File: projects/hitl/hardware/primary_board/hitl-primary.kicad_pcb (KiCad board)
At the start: 4 copper layers, 108 x 79.7 mm, 131 parts, among them J1 USB-Micro-1981568-1, J10 CONN_01X03, J11 CONN_01X03, J12 CONN_01X03, J13 CONN_01x02, J14 SSW-122-01-G-D, J15 CONN_01x02, J16 CONN_01X03, J17 CONN_01X03, J18 CONN_01X03, J19 CONN_01X03, J2 Barrel_jack, J20 CONN_01X03, J3 MM_F_VT_08_SM, J4 MM_F_VT_08_SM, J5 CONN_01x02, J6 DSub-9, J7 CONN_01X03, J8 CONN_01X03, J9 CONN_01X03, Q1 SSM3K333R, Q2 SSM3K333R, Q3 SSM3K333R, Q4 SSM3K333R, U1 R_500, U2 FT4222H, U3 PCA9306, U4 AD5675, U5 MAX7300AAXT, U6 RU_20_ADI, U7 MCP6001, U8 SOT109-1_NXP, U9 LT3045, Y1 Crystal_12MHz

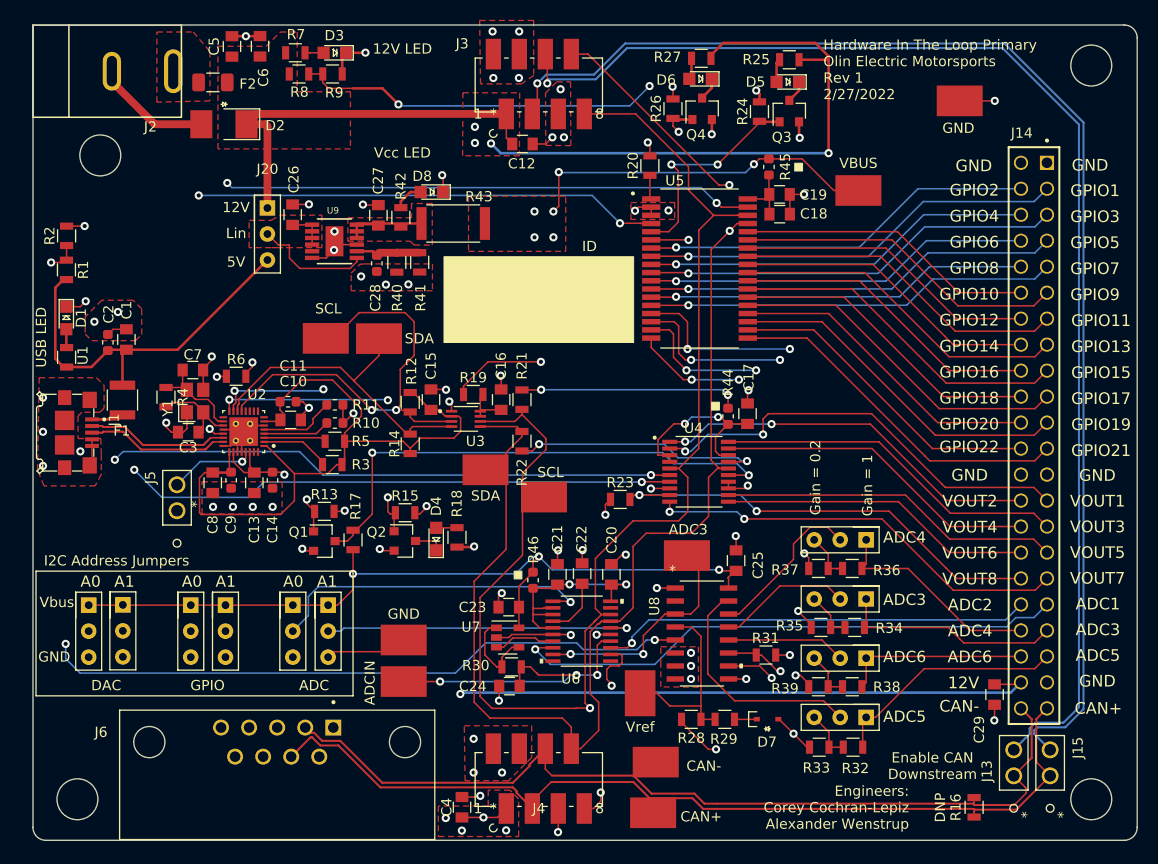
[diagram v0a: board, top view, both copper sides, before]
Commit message: Split schematic into sheets
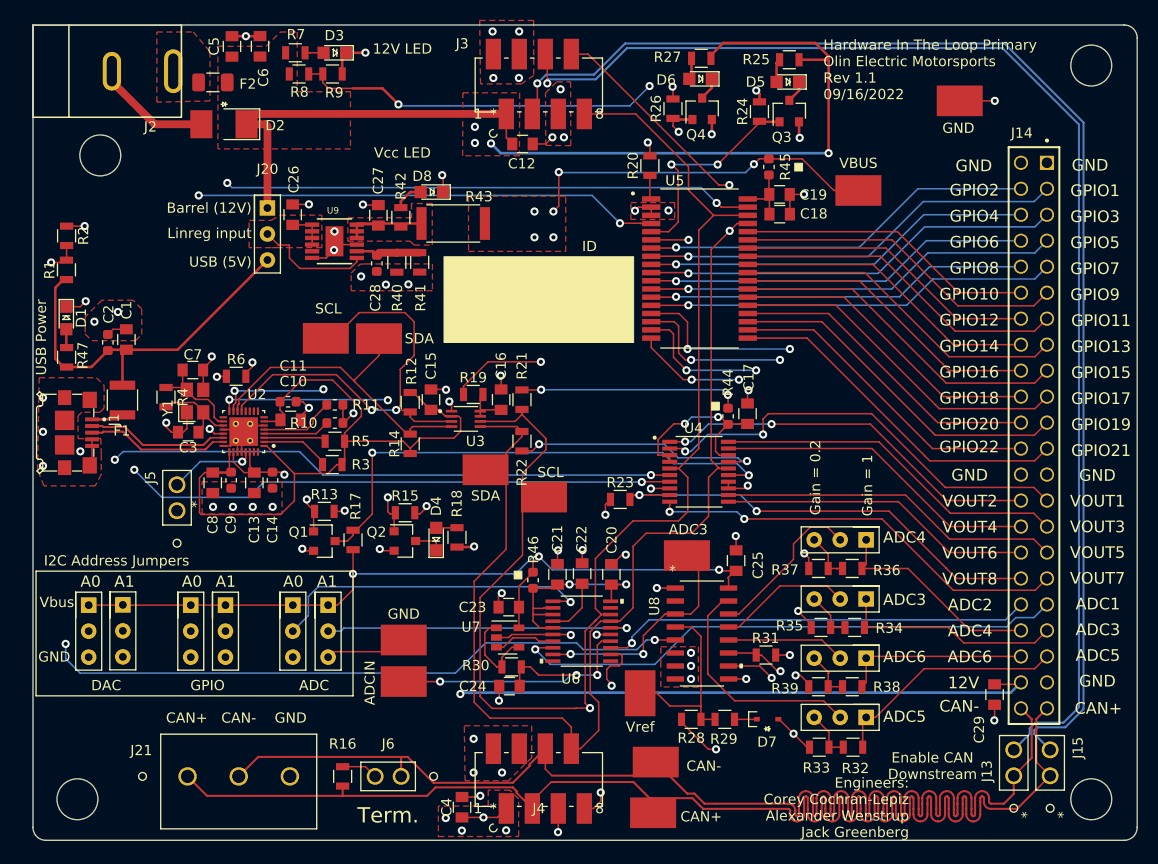
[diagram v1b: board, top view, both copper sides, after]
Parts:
- added J21: Screw_Terminal_01x03, footprints:ScrewPin_1x3, F.Cu at (87.7, 108.0)
- J6: value DSub-9 -> CONN_01x02; footprint footprints:TE_5745781-4 -> footprints:pinheader_1x2
- R16: value R_120_DNP -> R_120
- U6: value RU_20_ADI -> AD7091R-5BRUZ
- U8: value SOT109-1_NXP -> 74HCT4051D
- moved R16 61.8 mm to (102.9, 108.0)
- moved J6 12.6 mm to (108.6, 108.0), turned to 180 degrees
- turned R1 to 90 degrees
- turned R10 to 0 degrees
- turned R2 to -90 degrees
- renumbered U1 to R47
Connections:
- net /ADC-CA0 renamed /ADC Circuitry/ADC-CA0
- net /ADC-CA1 renamed /ADC Circuitry/ADC-CA1
- net /ADC1 renamed /ADC Circuitry/ADC1
- net /ADC2 renamed /ADC Circuitry/ADC2
- net /ADC4 renamed /ADC Circuitry/ADC_SELF_TEST
- net /Analog-MUX2 renamed /ADC Circuitry/ADC4
- net /Analog-MUX3 renamed /ADC Circuitry/ADC5
- net /Analog-MUX4 renamed /ADC Circuitry/ADC6
- net /Analog-MUX5 renamed /ADC Circuitry/ADC7
- net /CAN_AWAY+ renamed /Connectors/CAN_AWAY+
- net /CAN_AWAY- renamed /Connectors/CAN_AWAY-
- net /D+ renamed /USB->I2C/D+
- net /D- renamed /USB->I2C/D-
- net /DAC-A0 renamed /DAC/DAC-A0
- net /DAC-A1 renamed /DAC/DAC-A1
- net /DAC-LDAC renamed Net-(Q1-Pad3)
- net /FT-GPIO2 renamed /DAC/DAC-LDAC
- net /FT-GPIO3 renamed Net-(Q2-Pad1)
- net /FT-VPP renamed /USB->I2C/FT-VPP
- net /GPIO-10 renamed /Connectors/GPIO10
- net /GPIO-11 renamed /Connectors/GPIO11
- net /GPIO-12 renamed /Connectors/GPIO12
- net /GPIO-13 renamed /Connectors/GPIO13
- net /GPIO-14 renamed /Connectors/GPIO14
- net /GPIO-15 renamed /Connectors/GPIO15
- net /GPIO-16 renamed /Connectors/GPIO16
- net /GPIO-17 renamed /Connectors/GPIO17
- net /GPIO-18 renamed /Connectors/GPIO18
- net /GPIO-19 renamed /Connectors/GPIO19
- net /GPIO-20 renamed /Connectors/GPIO20
- net /GPIO-21 renamed /Connectors/GPIO21
- net /GPIO-22 renamed /Connectors/GPIO22
- net /GPIO-23 renamed /Connectors/GPIO23
- net /GPIO-24 renamed /Connectors/GPIO24
- net /GPIO-25 renamed /Connectors/GPIO25
- net /GPIO-26 renamed /Connectors/GPIO26
- net /GPIO-27 renamed /Connectors/GPIO27
- net /GPIO-28 renamed /Connectors/GPIO28
- net /GPIO-29 renamed /Connectors/GPIO29
- net /GPIO-30 renamed /Connectors/GPIO30
- net /GPIO-31 renamed /Connectors/GPIO31
- net /GPIO-4 renamed /Connectors/GPIO4
- net /GPIO-5 renamed /Connectors/GPIO5
- net /GPIO-6 renamed /Connectors/GPIO6
- net /GPIO-7 renamed /Connectors/GPIO7
- net /GPIO-8 renamed /Connectors/GPIO8
- net /GPIO-9 renamed /Connectors/GPIO9
- net /GPIO-AD0 renamed /GPIO/GPIO-AD0
- net /GPIO-AD1 renamed /GPIO/GPIO-AD1
- net /SCL renamed /Connectors/SCL
- net /SCL-FT renamed /USB->I2C/SDA
- net /SDA renamed /Connectors/SDA
- net /SDA-FT renamed /USB->I2C/SCL
- net /VOUT-1 renamed /Connectors/DAC1
- net /VOUT-2 renamed /Connectors/DAC2
- net /VOUT-3 renamed /Connectors/DAC3
- net /VOUT-4 renamed /Connectors/DAC4
- net /VOUT-5 renamed /Connectors/DAC5
- net /VOUT-6 renamed /Connectors/DAC6
- net /VOUT-7 renamed /Connectors/DAC7
- net /VOUT-8 renamed /Connectors/DAC8
- J13 pad 1: /CAN- -> /Connectors/CAN_N
- J14 pad 37: /Analog-MUX1 -> /ADC Circuitry/ADC3
- J14 pad 43: /CAN+ -> /Connectors/CAN_P
- J14 pad 44: /CAN- -> /Connectors/CAN_N
- J15 pad 1: /CAN+ -> /Connectors/CAN_P
- J17 pad 1: /Analog-MUX1 -> /ADC Circuitry/ADC3
- J4 pad 4: /CAN+ -> /Connectors/CAN_P
- J4 pad 5: /CAN- -> /Connectors/CAN_N
- J6 pad 1: Net-(J6-Pad1) -> /Connectors/CAN_N
- J6 pad 2: /CAN- -> Net-(J6-Pad2)
- R1 pad 1: /Analog-MUX6 -> +5V
- R1 pad 2: +5V -> /ADC Circuitry/Analog-MUX6
- R10 pad 1: GND -> Net-(R10-Pad1)
- R10 pad 2: Net-(R10-Pad2) -> GND
- R16 pad 1: /CAN+ -> /Connectors/CAN_P
- R16 pad 2: /CAN- -> Net-(J6-Pad2)
- R2 pad 1: /Analog-MUX6 -> GND
- R2 pad 2: GND -> /ADC Circuitry/Analog-MUX6
- R34 pad 1: /Analog-MUX1 -> /ADC Circuitry/ADC3
- TP11 pad 1: /ADC Circuitry/ADC3 -> /ADC Circuitry/ADC_MUX
- TP2 pad 1: /CAN+ -> /Connectors/CAN_P
- TP3 pad 1: /CAN- -> /Connectors/CAN_N
- U2 pad 10: Net-(U2-Pad10) -> unconnected-(U2-Pad10)
- U2 pad 11: Net-(U2-Pad11) -> unconnected-(U2-Pad11)
- U2 pad 12: Net-(U2-Pad12) -> unconnected-(U2-Pad12)
- U2 pad 17: Net-(U2-Pad17) -> unconnected-(U2-Pad17)
- U2 pad 31: Net-(U2-Pad31) -> unconnected-(U2-Pad31)
- U2 pad 32: Net-(U2-Pad32) -> unconnected-(U2-Pad32)
- U2 pad 4: Net-(R10-Pad2) -> Net-(R10-Pad1)
- U2 pad 8: Net-(U2-Pad8) -> unconnected-(U2-Pad8)
- U2 pad 9: Net-(U2-Pad9) -> unconnected-(U2-Pad9)
- U6 pad 10: Net-(U6-Pad10) -> unconnected-(U6-Pad10)
- U6 pad 11: Net-(U6-Pad11) -> unconnected-(U6-Pad11)
- U6 pad 19: Net-(U6-Pad19) -> unconnected-(U6-Pad19)
- U6 pad 9: /ADC Circuitry/ADC3 -> /ADC Circuitry/ADC_MUX
- U8 pad 2: /Analog-MUX7 -> unconnected-(U8-Pad2)
- U8 pad 3: /ADC Circuitry/ADC3 -> /ADC Circuitry/ADC_MUX
- U8 pad 5: /Analog-MUX6 -> /ADC Circuitry/Analog-MUX6
- U9 pad 5: Net-(U9-Pad5) -> unconnected-(U9-Pad5)
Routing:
- net /Connectors/CAN_P: track 0.00 -> 143.5 mm
- net /Connectors/CAN_N: track 0.00 -> 140.0 mm
- net /Analog-MUX6: track 104.4 -> 0.00 mm, vias 3 -> 0
- net /ADC Circuitry/Analog-MUX6: track 0.00 -> 104.4 mm, vias 0 -> 3
- net /CAN+: track 90.2 -> 0.00 mm
- net /CAN-: track 88.8 -> 0.00 mm
- net /ADC Circuitry/ADC_MUX: track 0.00 -> 22.7 mm, vias 0 -> 2
- net /Analog-MUX1: track 21.8 -> 0.00 mm
- net Net-(R10-Pad2): track 6.56 -> 0.00 mm
- net Net-(R10-Pad1): track 0.00 -> 6.56 mm
- net Net-(J6-Pad2): track 0.00 -> 3.57 mm
- net /ADC Circuitry/ADC3: track 22.7 -> 21.8 mm, vias 2 -> 0
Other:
- board text added: "Barrel (12V)"
- board text added: "Engineers: Corey Cochran-Lepiz Alexander Wenstrup Jack Greenberg"
- board text added: "Hardware In The Loop Primary Olin Electric Motorsports Rev 1.1 09/16/2022"
- board text added: "Linreg input"
- board text added: "Term."
- board text added: "USB (5V)"
- board text added: "USB Power"
- board text removed: "5V"
- board text removed: "DNP"
- board text removed: "Engineers: Corey Cochran-Lepiz Alexander Wenstrup"
- board text removed: "Hardware In The Loop Primary Olin Electric Motorsports Rev 1 2/27/2022"
- board text removed: "Lin"
- board text removed: "USB LED"

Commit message: Switch FTPROG to button and update I2C level shifter
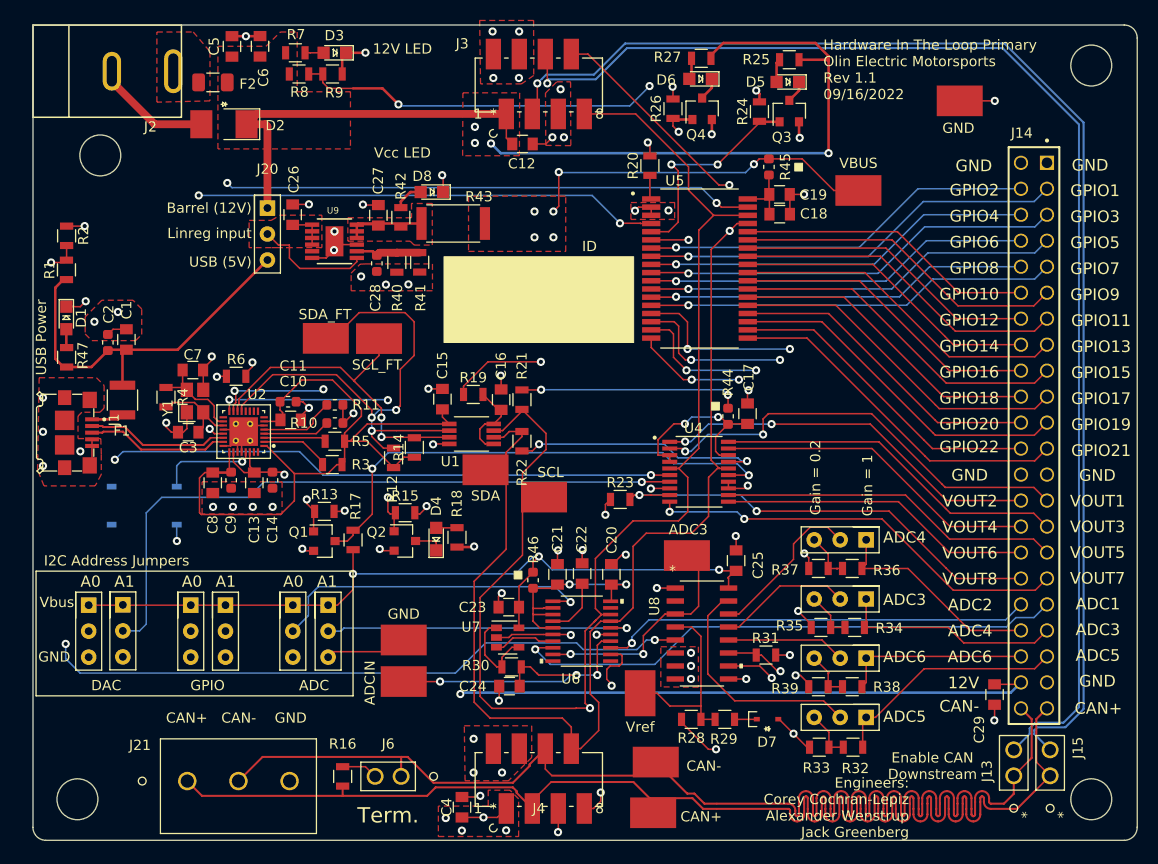
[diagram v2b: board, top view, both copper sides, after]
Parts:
- removed J5: CONN_01x02, footprints:pinheader_1x2
- removed U3: PCA9306, footprints:SOP50P310X90-8N_pca9306
- added SW1: SW_SPST, footprints:Button_PTS526, B.Cu at (83.5, 81.5)
- added U1: PCA9517, footprints:Micro8_PCA9517, F.Cu at (115.5, 74.5)
- moved R12 5.67 mm to (107.8, 76.8), turned to 90 degrees
- moved C15 1.12 mm to (112.6, 71.1)
- moved R14 0.54 mm to (109.9, 75.8)
- moved J21 0.46 mm to (87.7, 108.4)
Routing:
- net /USB->I2C/SDA: track 43.9 -> 50.8 mm, vias 2 -> 3
- net /DAC/DAC-A1: track 70.3 -> 65.9 mm, vias 2 -> 1
- net Net-(C16-Pad1): track 4.34 -> 8.52 mm
- net GND: track 135.0 -> 137.0 mm, vias 72 -> 73
- net /USB->I2C/FT-VPP: track 8.39 -> 9.70 mm
- net /Connectors/SDA: track 138.8 -> 137.5 mm
- net /USB->I2C/SCL: track 31.8 -> 32.7 mm, vias 0 -> 2
- net Net-(Q1-Pad3): track 50.8 -> 49.8 mm
- net +3V3: track 70.4 -> 71.3 mm
- net /Connectors/SCL: track 142.3 -> 141.6 mm
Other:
- board text added: "FT Prog"
- board text added: "SCL_FT"
- board text added: "SDA_FT"
